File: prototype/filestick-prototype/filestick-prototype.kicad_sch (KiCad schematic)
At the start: 16 parts

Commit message: fix clk pins
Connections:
- net CLK+: now also J?.5 (CLK+); no longer J?.3 (CLK+)
- net CLK-: now also J?.3 (CLK-); no longer J?.5 (CLK-)
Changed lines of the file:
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@@
-    (stroke (width 0) (type default) (color 0 0 0 0))
-  )
-  (wire (pts (xy 250.19 134.62) (xy 256.54 134.62))
     (stroke (width 0) (type default) (color 0 0 0 0))
   )
@@
     (stroke (width 0) (type default) (color 0 0 0 0))
   )
-  (wire (pts (xy 246.38 153.67) (xy 246.38 129.54))
-    (stroke (width 0) (type default) (color 0 0 0 0))
-  )
   (wire (pts (xy 198.12 116.84) (xy 198.12 105.41))
     (stroke (width 0) (type default) (color 0 0 0 0))
@@
     (stroke (width 0) (type default) (color 0 0 0 0))
   )
+  (wire (pts (xy 250.19 129.54) (xy 256.54 129.54))
+    (stroke (width 0) (type default) (color 0 0 0 0))
+  )
   (wire (pts (xy 181.61 119.38) (xy 205.74 119.38))
     (stroke (width 0) (type default) (color 0 0 0 0))
@@
     (stroke (width 0) (type default) (color 0 0 0 0))
   )
-  (wire (pts (xy 246.38 129.54) (xy 256.54 129.54))
-    (stroke (width 0) (type default) (color 0 0 0 0))
-  )
-  (wire (pts (xy 250.19 148.59) (xy 250.19 134.62))
+  (wire (pts (xy 254 153.67) (xy 254 134.62))
     (stroke (width 0) (type default) (color 0 0 0 0))
   )
@@
     (stroke (width 0) (type default) (color 0 0 0 0))
   )
+  (wire (pts (xy 250.19 148.59) (xy 250.19 129.54))
+    (stroke (width 0) (type default) (color 0 0 0 0))
+  )
   (wire (pts (xy 198.12 105.41) (xy 207.01 105.41))
     (stroke (width 0) (type default) (color 0 0 0 0))
@@
     (stroke (width 0) (type default) (color 0 0 0 0))
   )
-  (wire (pts (xy 223.52 153.67) (xy 246.38 153.67))
+  (wire (pts (xy 223.52 153.67) (xy 254 153.67))
     (stroke (width 0) (type default) (color 0 0 0 0))
   )
@@
   )
   (wire (pts (xy 201.93 152.4) (xy 205.74 152.4))
+    (stroke (width 0) (type default) (color 0 0 0 0))
+  )
+  (wire (pts (xy 254 134.62) (xy 256.54 134.62))
     (stroke (width 0) (type default) (color 0 0 0 0))
   )
@@
     )
     (pin "1")
+    (pin "2")
+    (pin "3")
     (pin "4")
-    (pin "2")
     (pin "5")
-    (pin "3")
   )
   (symbol (lib_id "filestick_ic_lib:SN65HVD75") (at 214.63 143.51 0) (unit 1)

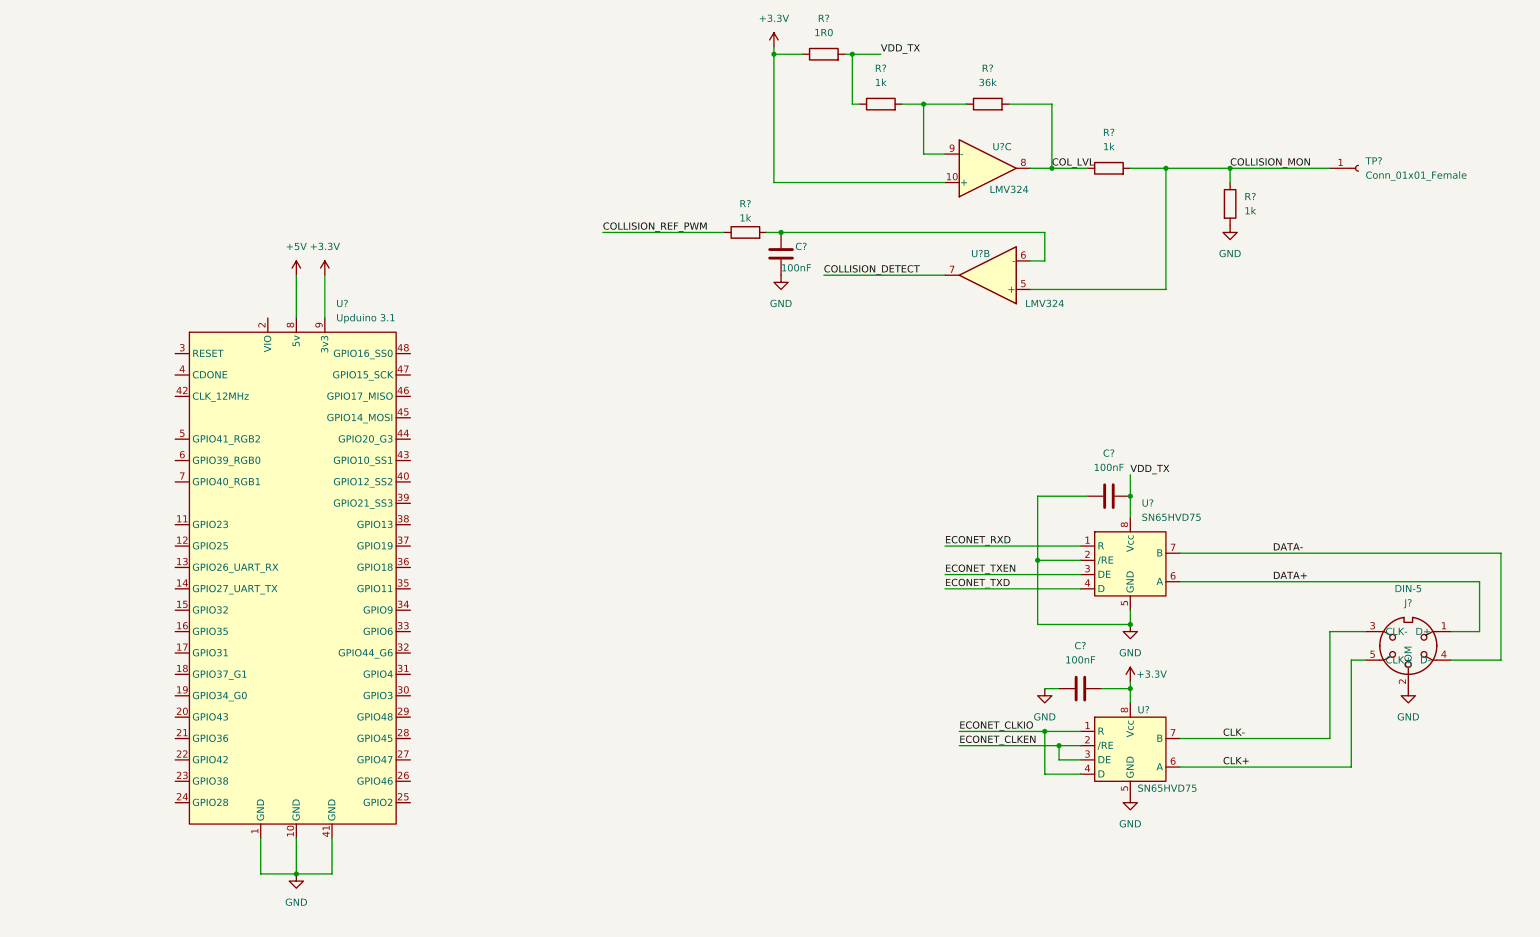
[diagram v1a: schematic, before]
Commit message: add termination circuit
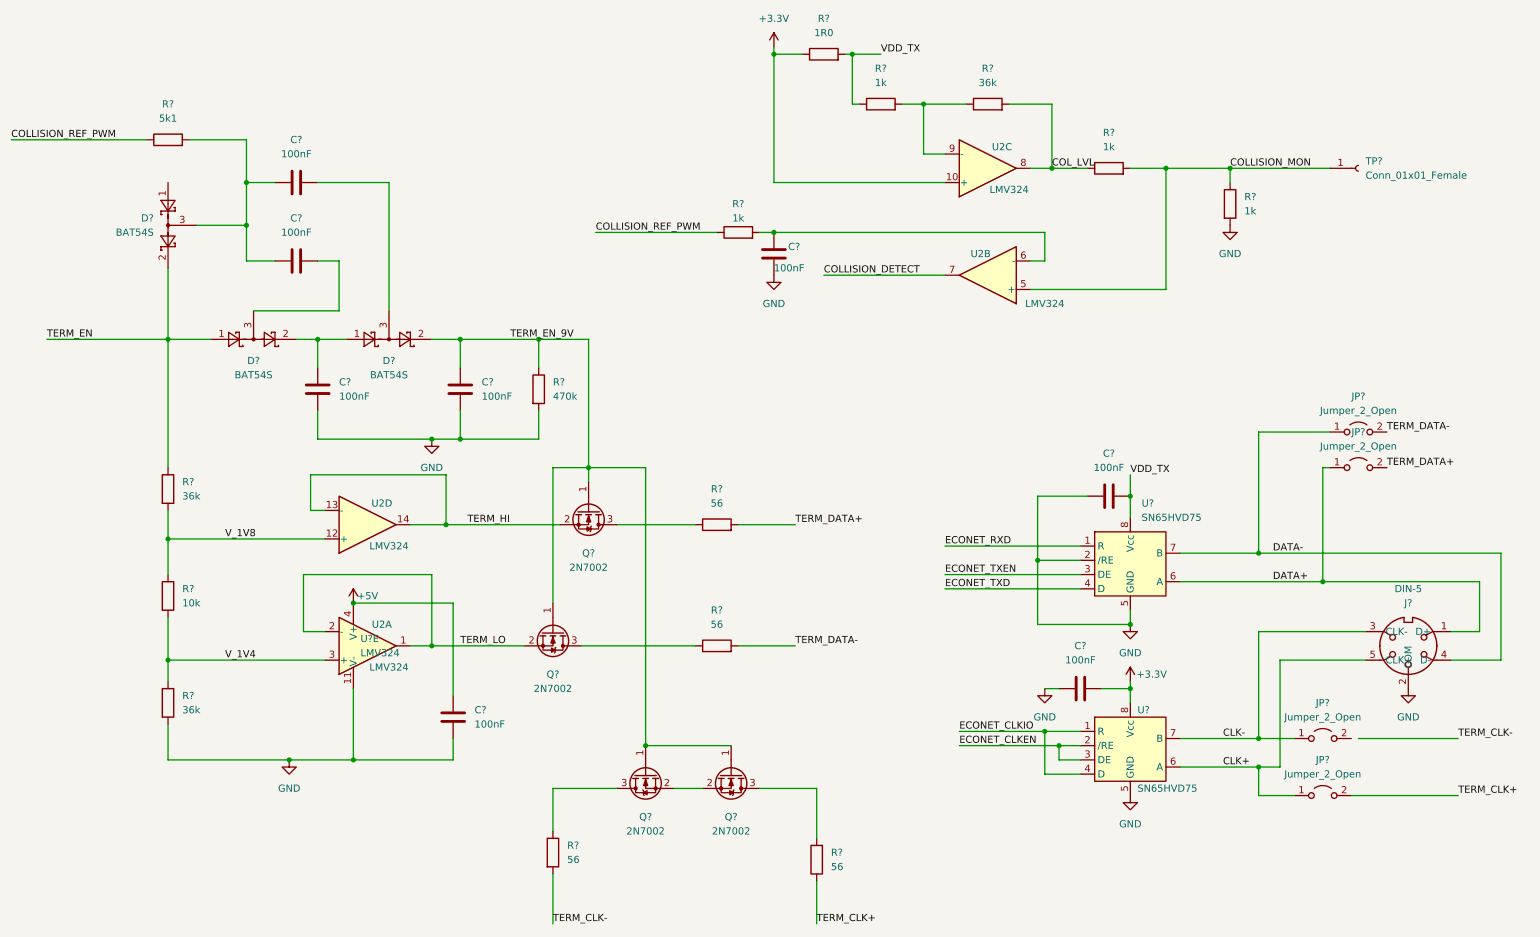
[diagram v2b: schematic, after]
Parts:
- removed U?: Upduino 3.1, Package_DIP:DIP-48_W15.24mm_Socket, symbol filestick_ic_lib:Upduino 3.1
- added C? (x5): 100nF, symbol Device:C
- added D? (x3): BAT54S, Package_TO_SOT_SMD:SOT-23, symbol Diode:BAT54S
- added JP? (x4): Jumper_2_Open, symbol Jumper:Jumper_2_Open
- added Q? (x4): 2N7002, Package_TO_SOT_SMD:SOT-23, symbol Transistor_FET:2N7002
- added R?: 470k, symbol Device:R
- added R? (x2): 36k, symbol Device:R
- added R?: 5k1, symbol Device:R
- added R? (x4): 56, symbol Device:R
- added R?: 10k, symbol Device:R
- added unit 4 of U2
- added unit 1 of U2
- added U?: LMV324, symbol Amplifier_Operational:LMV324
- gave numbers to parts that had none: 1
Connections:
- net +5V: now also C?.1, U?.4 (V+)
- net CLK+: now also JP?.1 (A)
- net CLK-: now also JP?.1 (A)
- net COLLISION_REF_PWM: now also R?.1
- net DATA+: now also JP?.1 (A)
- net DATA-: now also JP?.1 (A)
- net GND: now also C?.2, C?.2, C?.2, R?.2, R?.2, U?.11 (V-)
- new net: C?.1, C?.1, D?.3, R?.2
- new net: Q?.3 (D), R?.1 (x3)
- new net: C?.1, D?.1, D?.2
- new net: C?.2, D?.3 (x2)
- new net: Q?.2 (S), Q?.2 (S)
- new net: Q?.3 (D), R?.2
- new net TERM_CLK+: JP?.2 (B), R?.1
- new net TERM_CLK-: R?.2
- new net TERM_DATA+: JP?.2 (B), R?.2
- new net TERM_DATA-: JP?.2 (B), R?.2
- new net TERM_EN: D?.1, D?.2, R?.1
- new net TERM_EN_9V: C?.1, D?.2, Q?.1 (G), Q?.1 (G), Q?.1 (G), Q?.1 (G), R?.1
- new net TERM_HI: Q?.2 (S), U2.13 (-), U2.14
- new net TERM_LO: Q?.2 (S), U2.1, U2.2 (-)
- new net V_1V4: R?.1, R?.2, U2.3 (+)
- new net V_1V8: R?.1, R?.2, U2.12 (+)
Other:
- moved on the sheet: C?, R?

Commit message: schematic save
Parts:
- added TP?: Conn_01x01_Female, symbol Connector:Conn_01x01_Female
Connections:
- net TERM_EN_9V: now also TP?.1 (Pin_1)
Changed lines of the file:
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@@
   (junction (at 95.25 95.25) (diameter 0) (color 0 0 0 0)
+  )
+  (junction (at 118.11 77.47) (diameter 0) (color 0 0 0 0)
   )
   (junction (at 237.49 153.67) (diameter 0) (color 0 0 0 0)
@@
     (pin "2")
   )
+  (symbol (lib_id "Connector:Conn_01x01_Female") (at 123.19 77.47 0) (unit 1)
+    (in_bom yes) (on_board yes) (fields_autoplaced)
+    (property "Reference" "TP?" (id 0) (at 124.46 76.1999 0)
+      (effects (font (size 1.27 1.27)) (justify left))
+    )
+    (property "Value" "Conn_01x01_Female" (id 1) (at 124.46 78.7399 0)
+      (effects (font (size 1.27 1.27)) (justify left))
+    )
+    (property "Footprint" "" (id 2) (at 123.19 77.47 0)
+      (effects (font (size 1.27 1.27)) hide)
+    )
+    (property "Datasheet" "~" (id 3) (at 123.19 77.47 0)
+      (effects (font (size 1.27 1.27)) hide)
+    )
+    (pin "1")
+  )
   (sheet_instances
     (path "/" (page "1"))
@@
       (reference "TP?") (unit 1) (value "Conn_01x01_Female") (footprint "")
     )
+    (path "/fdec3421-c7db-441a-bb89-5d9ad1a7c793"
+      (reference "TP?") (unit 1) (value "Conn_01x01_Female") (footprint "")
+    )

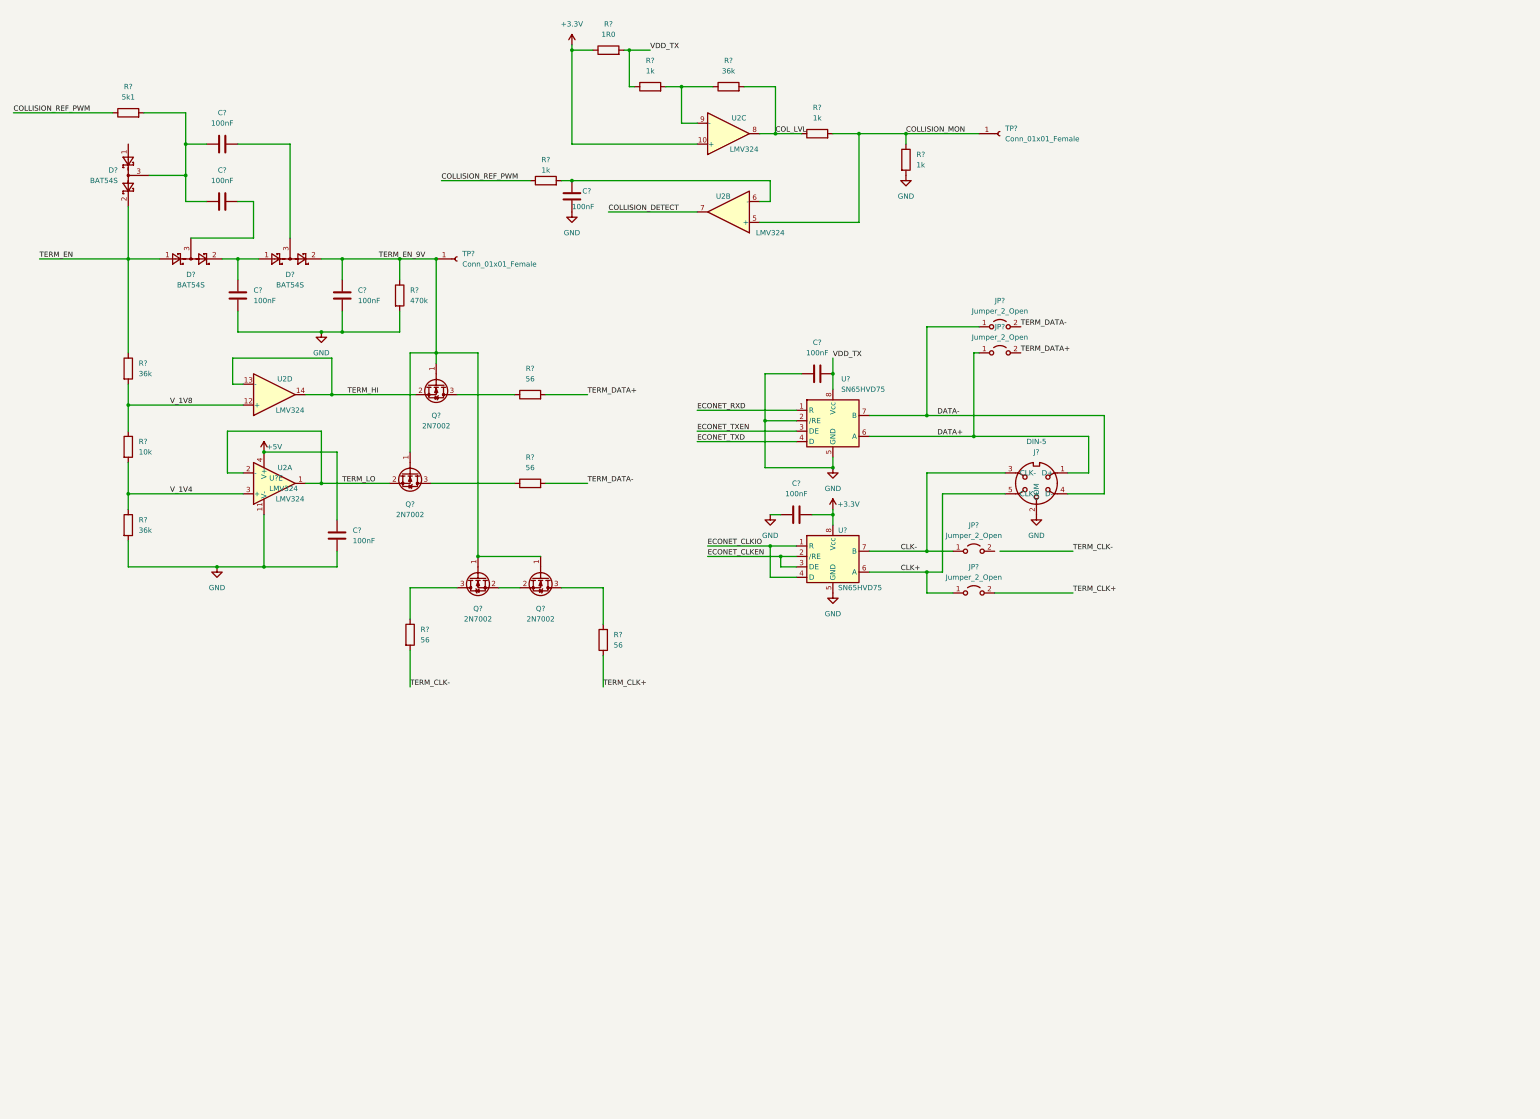
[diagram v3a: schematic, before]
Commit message: Add symbol for SD card breakout board
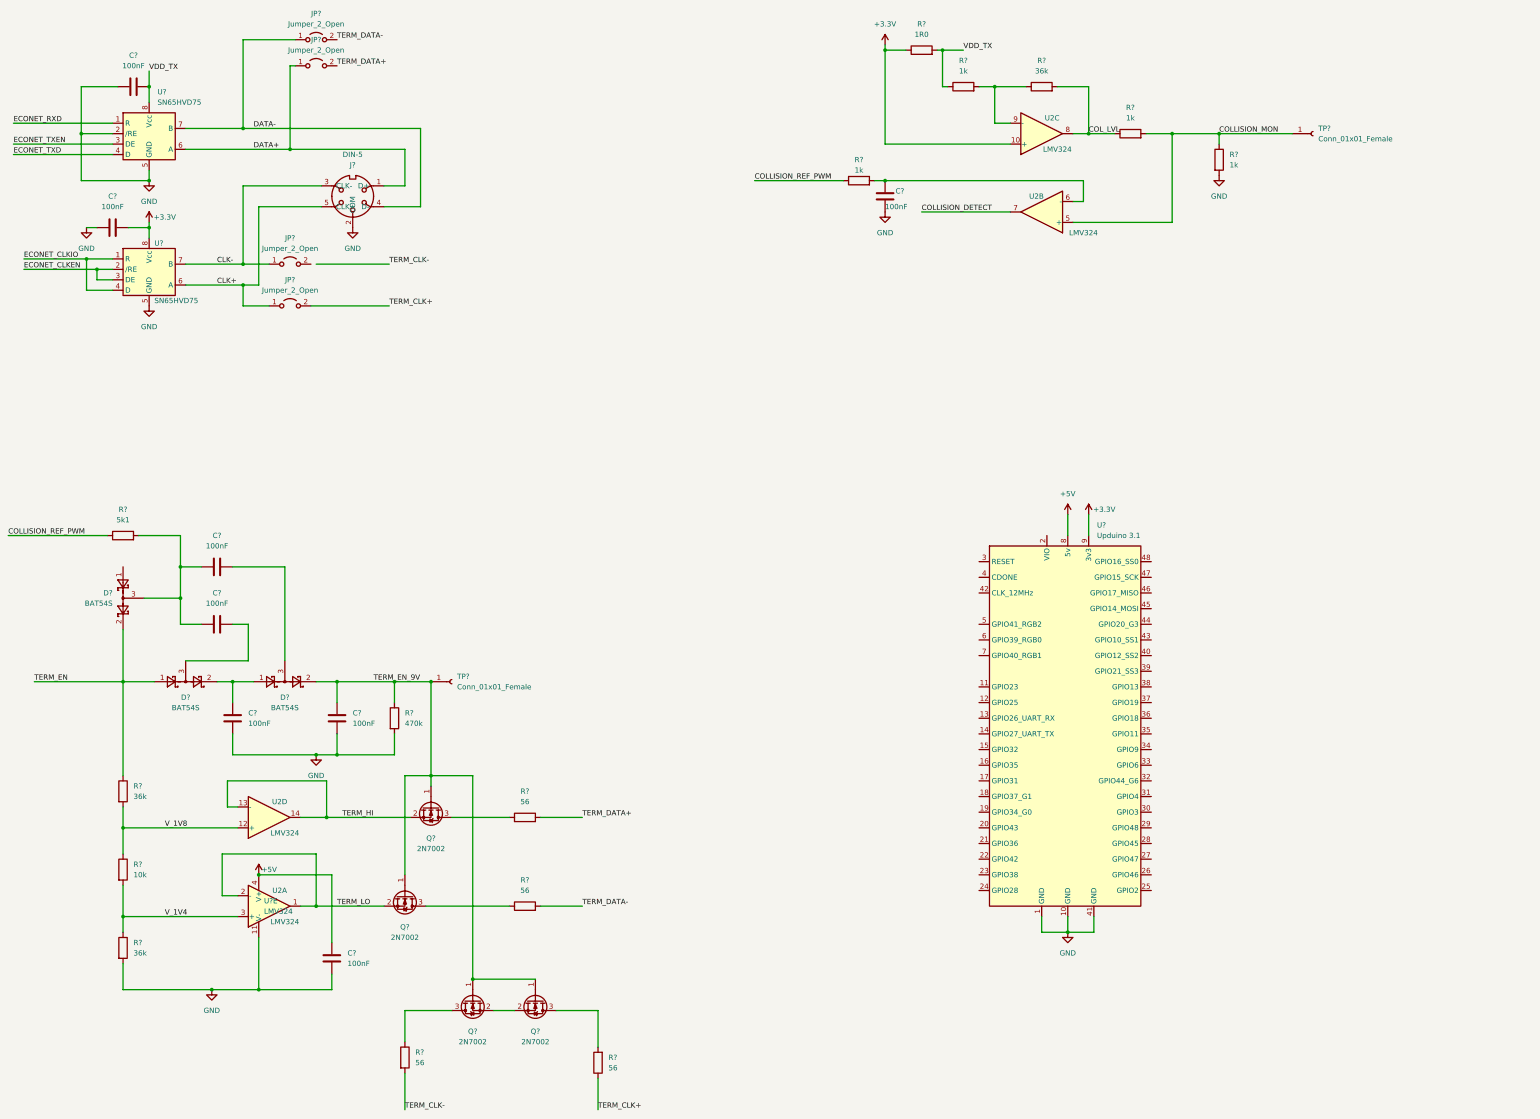
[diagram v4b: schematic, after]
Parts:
- added U?: Upduino 3.1, Package_DIP:DIP-48_W15.24mm_Socket, symbol filestick_ic_lib:Upduino 3.1
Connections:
- net +3.3V: now also U?.9 (3v3)
- net +5V: now also U?.8 (5v)
- net GND: now also U?.1 (GND), U?.10 (GND), U?.41 (GND)
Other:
- moved on the sheet: C?, D?, J?, JP?, Q?, R?, TP?, U2A, U2B, U2C, U2D, U?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

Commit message: more schematic
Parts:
- added J?: Conn_01x07_Male, symbol Connector:Conn_01x07_Male
- added J?: Conn_01x05_Male, symbol Connector:Conn_01x05_Male
- added J?: DIN-5, symbol Connector:DIN-5
- added R? (x2): 1k, symbol Device:R
- added SW?: SW_Push, symbol Switch:SW_Push
- added TP?: Conn_01x01_Female, symbol Connector:Conn_01x01_Female
- added U?: pololu_sd_breakout, filestick-footprints:pololu_sd_card, symbol filestick_ic_lib:pololu_sd_breakout
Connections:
- net +3.3V: now also R?.1, U?.10 (Vdd), U?.2 (Vdd)
- net CLK+: now also J?.5 (CLK+)
- net CLK-: now also J?.3 (CLK-)
- net COLLISION_DETECT: now also U?.15 (GPIO32)
- net COLLISION_REF_PWM: now also U?.17 (GPIO31)
- net DATA+: now also J?.4 (D-)
- net DATA-: now also J?.1 (D+)
- net ECONET_CLKEN: now also U?.23 (GPIO38), R?.1
- net ECONET_CLKIO: now also U?.19 (GPIO34_G0)
- net ECONET_RXD: now also U?.20 (GPIO43)
- net ECONET_TXD: now also U?.21 (GPIO36)
- net ECONET_TXEN: now also U?.22 (GPIO42)
- net GND: now also J?.1 (Pin_1), J?.2 (COM), R?.2, SW?.1, U?.1 (GND), U?.11 (GND)
- net TERM_CLK-: now also JP?.2 (B)
- net TERM_EN: now also U?.16 (GPIO35)
- net at U?.11 (GPIO23): now also J?.6 (Pin_6)
- net at U?.12 (GPIO25): now also J?.7 (Pin_7)
- net at U?.13 (GPIO26_UART_RX): now also J?.4 (Pin_4)
- net at U?.14 (GPIO27_UART_TX): now also J?.5 (Pin_5)
- net at U?.2 (VIO): now also J?.1 (Pin_1)
- net at U?.3 (RESET): now also SW?.2
- net at U?.38 (GPIO13): now also R?.2, U?.7 (CD)
- net at U?.4 (CDONE): now also J?.2 (Pin_2)
- net at U?.42 (CLK_12MHz): now also TP?.1 (Pin_1)
- net at U?.43 (GPIO10_SS1): now also U?.6 (/CS)
- net at U?.45 (GPIO14_MOSI): now also U?.3 (DI)
- net at U?.46 (GPIO17_MISO): now also U?.4 (DO)
- net at U?.47 (GPIO15_SCK): now also U?.5 (SCLK)
- net at U?.5 (GPIO41_RGB2): now also J?.3 (Pin_3)
- net at U?.6 (GPIO39_RGB0): now also J?.4 (Pin_4)
- net at U?.7 (GPIO40_RGB1): now also J?.5 (Pin_5)
- no-connect marks 0 -> 2
